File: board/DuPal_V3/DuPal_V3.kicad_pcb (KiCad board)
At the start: 2 copper layers, 116.8 x 73.7 mm, 132 parts, among them J1 ZIF Socket, J2 Debug Header, J3 Extra, J4 Conn_01x21_Pin, J5 Conn_01x21_Pin, K1 G6K-2, Q1 2N3904, SW1 RESET, U1 Pico, U10 74HCT166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

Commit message: Add gerbers for rev1 of dupal v3
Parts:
- added G***: LOGO, logo:logo, F.Cu at (192.5, 49.1)
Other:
- board text added: "DuPAL V3"
- board text added: "Extra GND"

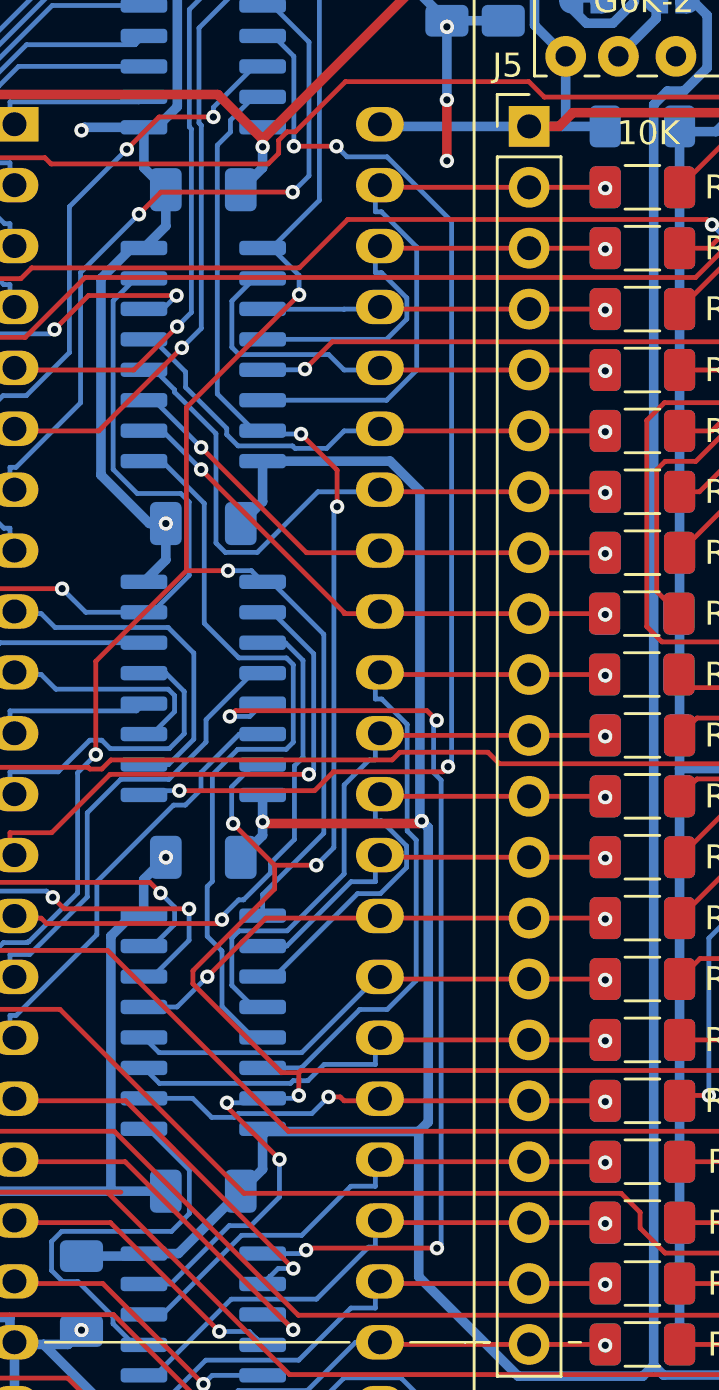
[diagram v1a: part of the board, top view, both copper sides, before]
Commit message: Begin cleaning up some egregious clearance rule violations
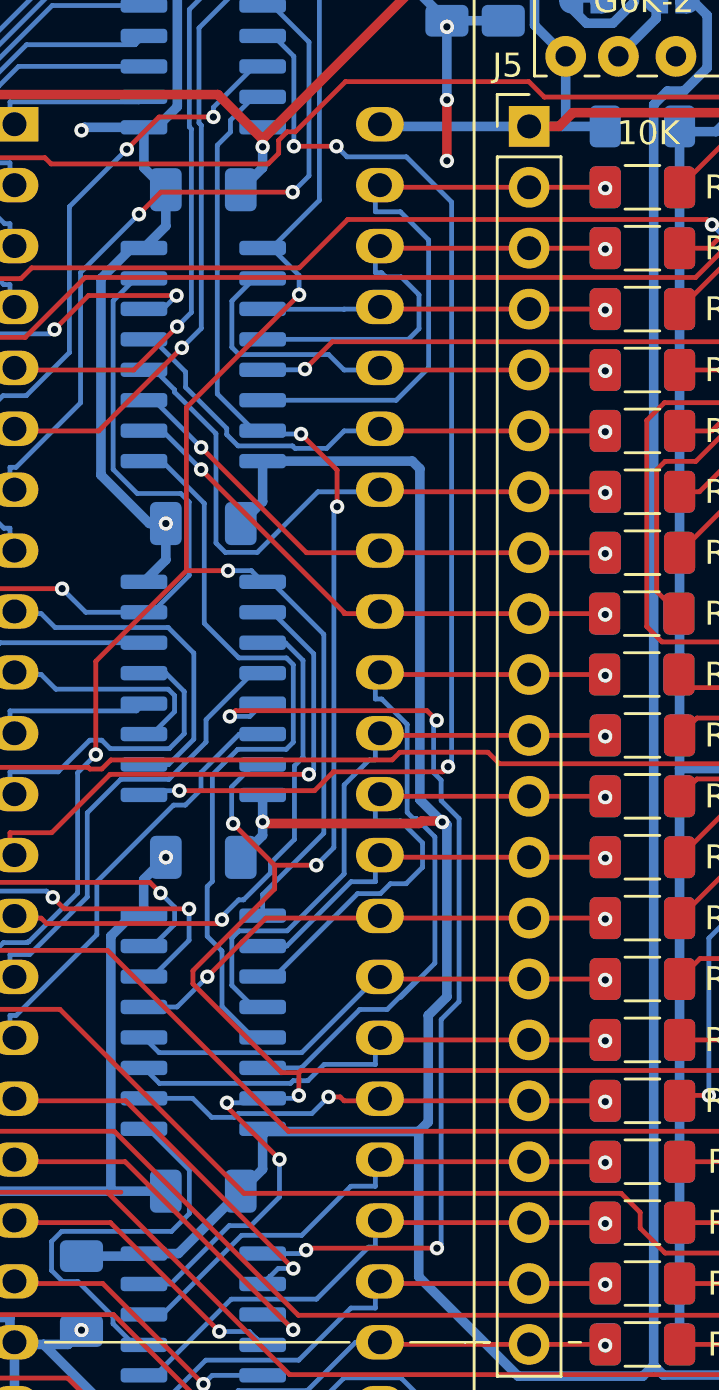
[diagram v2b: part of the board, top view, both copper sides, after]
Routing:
- net VCC: track 326.8 -> 328.9 mm
- net /ZIF_33: track 31.5 -> 33.2 mm
- net /ZIF_31: track 21.5 -> 22.9 mm
- net /ZIF_40: track 20.0 -> 21.3 mm
- net /ZIF_41: track 25.4 -> 26.5 mm
- net Net-(U10-Ds): track 40.1 -> 40.7 mm

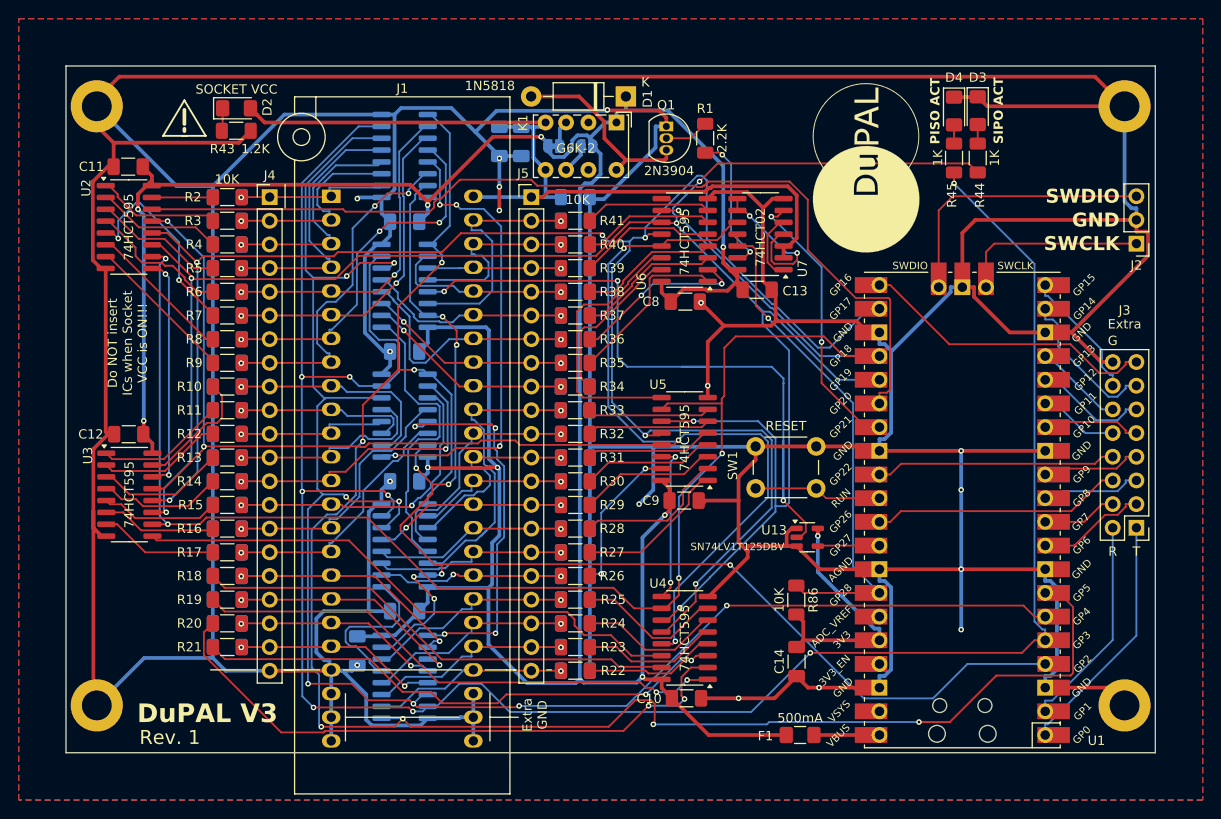
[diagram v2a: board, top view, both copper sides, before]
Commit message: Avoid clearance violations, create rev.2 board for dupico
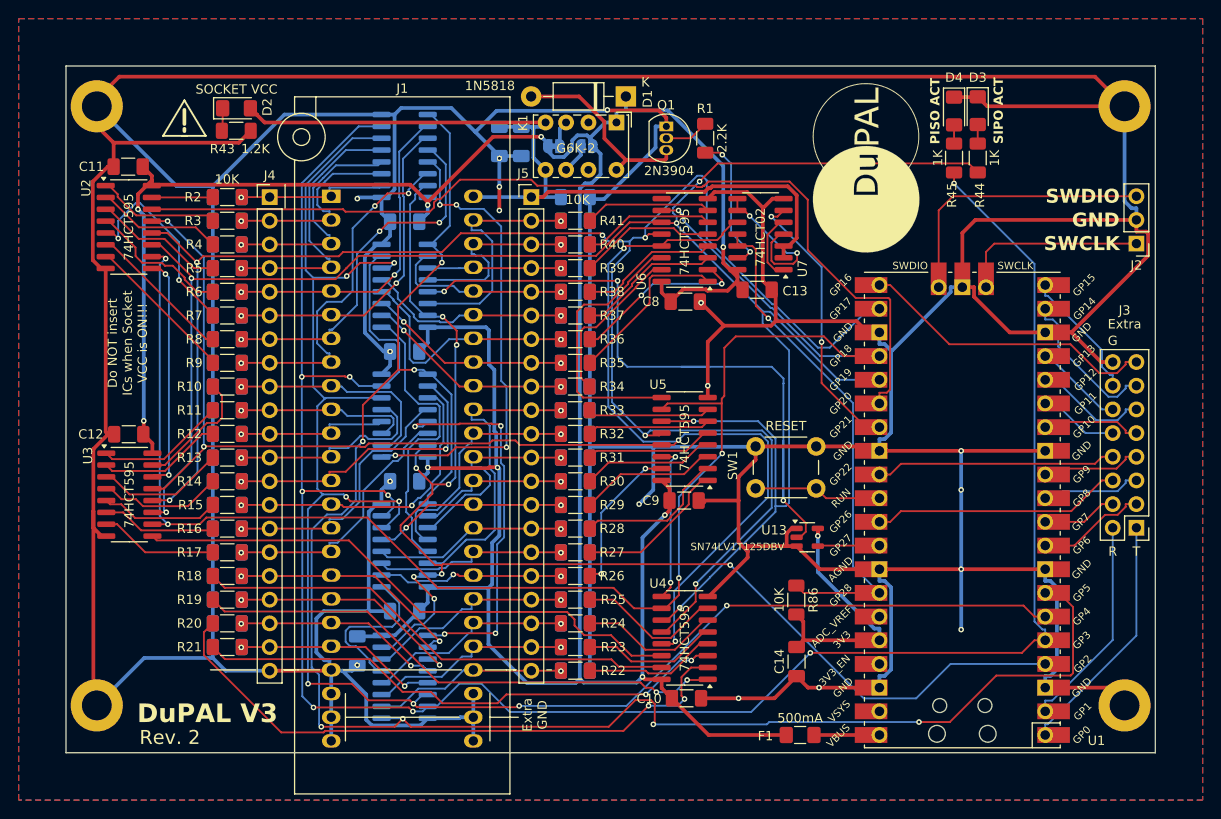
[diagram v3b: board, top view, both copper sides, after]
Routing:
- net Net-(U8-Qh): track 49.7 -> 50.7 mm
- net Net-(U4-QB): track 58.3 -> 57.8 mm
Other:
- board text added: "Rev. 2"
- board text removed: "Rev. 1"
